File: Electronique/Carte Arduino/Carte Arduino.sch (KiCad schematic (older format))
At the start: 12 parts

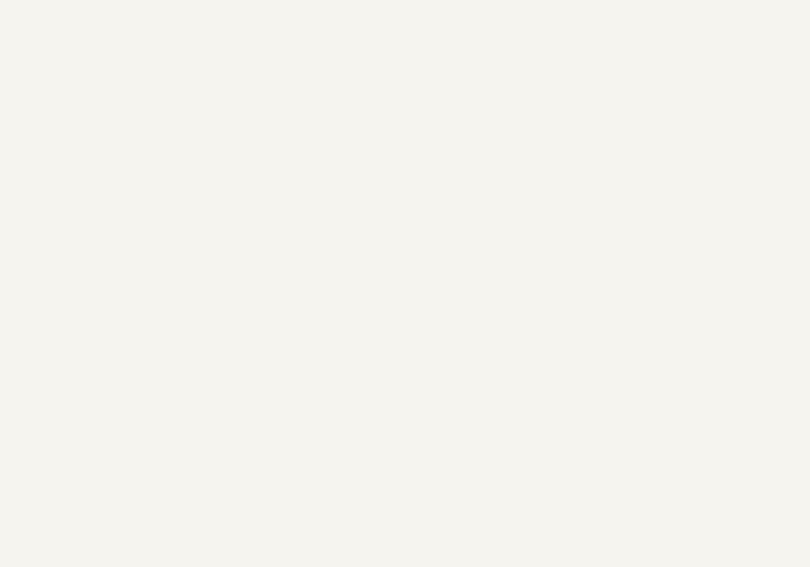
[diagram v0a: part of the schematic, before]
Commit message: Electronique/Carte Arduino/Carte Arduino.sch : - Ajout des connecteurs pour les capteurs de Co2 et de CH4
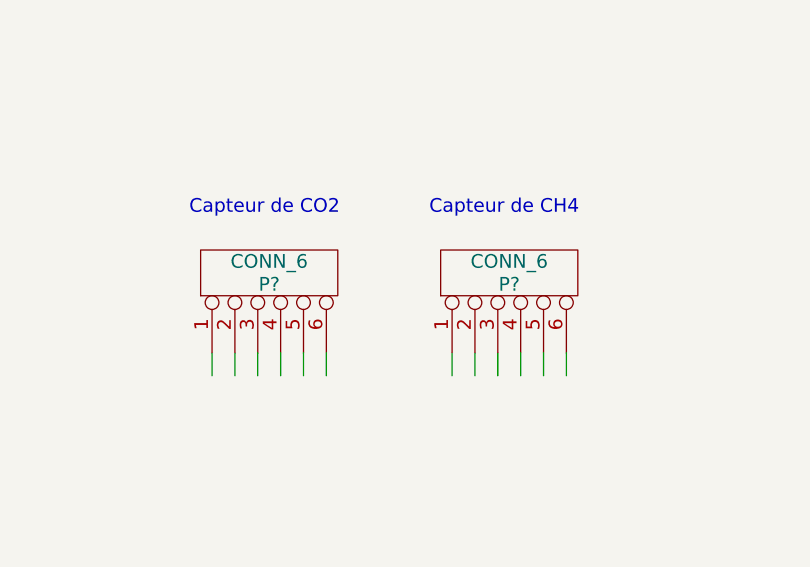
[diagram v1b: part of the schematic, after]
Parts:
- added P? (x2): CONN_6, symbol CONN_6
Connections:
- wire segments 39 -> 51
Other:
- note added: "Capteur de CH4"
- note added: "Capteur de CO2"
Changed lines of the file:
@@
-EESchema Schematic File Version 2  date 12/12/2011 20:48:11
+EESchema Schematic File Version 2  date 12/12/2011 22:18:57
 LIBS:power
 LIBS:device
@@
 Comment4 ""
 $EndDescr
+Wire Wire Line
+	5400 3950 5400 4050
+Wire Wire Line
+	5200 3950 5200 4050
+Wire Wire Line
+	5000 3950 5000 4050
+Wire Wire Line
+	4350 3950 4350 4050
+Wire Wire Line
+	4150 3950 4150 4050
+Wire Wire Line
+	3950 3950 3950 4050
+Wire Wire Line
+	7750 6550 7850 6550
+Wire Wire Line
+	9550 6350 9650 6350
+Wire Wire Line
+	9550 6450 9650 6450
+Wire Wire Line
+	7850 5900 7750 5900
+Wire Wire Line
+	5950 6400 5950 6500
+Wire Wire Line
+	5750 6400 5750 6500
+Wire Wire Line
+	5550 6400 5550 6500
+Wire Wire Line
+	5150 6400 5150 6500
+Wire Wire Line
+	4950 6400 4950 6500
+Wire Wire Line
+	4750 6400 4750 6500
+Wire Wire Line
+	4550 6400 4550 6500
+Wire Wire Line
+	4150 6400 4150 6500
+Wire Wire Line
+	3950 6400 3950 6500
+Wire Wire Line
+	2100 5350 2100 5500
+Wire Wire Line
+	2100 4750 2100 4850
+Wire Wire Line
+	2300 4850 2300 4750
+Wire Wire Line
+	1900 4850 1900 4750
+Wire Wire Line
+	1700 4750 1700 4850
+Wire Wire Line
+	1700 5350 1700 5500
+Wire Wire Line
+	1300 5350 1300 5500
+Wire Wire Line
+	1300 4750 1300 4850
+Wire Wire Line
+	1500 4850 1500 4750
+Wire Wire Line
+	1100 4850 1100 4750
+Wire Wire Line
+	900  4750 900  4850
+Wire Wire Line
+	900  5350 900  5500
+Wire Wire Line
+	3850 6400 3850 6500
+Wire Wire Line
+	4050 6400 4050 6500
+Wire Wire Line
+	4450 6400 4450 6500
+Wire Wire Line
+	4650 6400 4650 6500
+Wire Wire Line
+	4850 6400 4850 6500
+Wire Wire Line
+	5050 6400 5050 6500
+Wire Wire Line
+	5450 6400 5450 6500
+Wire Wire Line
+	5650 6400 5650 6500
+Wire Wire Line
+	5850 6400 5850 6500
+Wire Wire Line
+	6050 6400 6050 6500
+Wire Wire Line
+	6150 6400 6150 6500
+Wire Wire Line
+	9550 6500 9650 6500
+Wire Wire Line
+	9550 6400 9650 6400
+Wire Wire Line
+	7850 6500 7750 6500
+Wire Wire Line
+	3850 3950 3850 4050
+Wire Wire Line
+	4050 3950 4050 4050
+Wire Wire Line
+	4250 3950 4250 4050
+Wire Wire Line
+	4900 3950 4900 4050
+Wire Wire Line
+	5100 3950 5100 4050
+Wire Wire Line
+	5300 3950 5300 4050
+Text Notes 4800 3350 0    60   ~ 0
+Capteur de CH4
+Text Notes 3750 3350 0    60   ~ 0
+Capteur de CO2
+$Comp
+L CONN_6 P?
+U 1 1 4EE66058
+P 5150 3600
+F 0 "P?" V 5100 3600 60  0000 C CNN
+F 1 "CONN_6" V 5200 3600 60  0000 C CNN
+	1    5150 3600
+	0    -1   -1   0
+$EndComp
+$Comp
+L CONN_6 P?
+U 1 1 4EE66049
+P 4100 3600
+F 0 "P?" V 4050 3600 60  0000 C CNN
+F 1 "CONN_6" V 4150 3600 60  0000 C CNN
+	1    4100 3600
+	0    -1   -1   0
+$EndComp
 NoConn ~ 5950 6500
 NoConn ~ 5850 6500
@@
 Text Notes 8550 5750 0    60   ~ 0
 Arduino
-Wire Wire Line
-	7750 6550 7850 6550
-Wire Wire Line
-	9550 6350 9650 6350
-Wire Wire Line
-	9550 6450 9650 6450
-Wire Wire Line
-	7850 5900 7750 5900
-Wire Wire Line
-	5950 6400 5950 6500
-Wire Wire Line
-	5750 6400 5750 6500
-Wire Wire Line
-	5550 6400 5550 6500
-Wire Wire Line
-	5150 6400 5150 6500
-Wire Wire Line
-	4950 6400 4950 6500
-Wire Wire Line
-	4750 6400 4750 6500
-Wire Wire Line
-	4550 6400 4550 6500
-Wire Wire Line
-	4150 6400 4150 6500
-Wire Wire Line
-	3950 6400 3950 6500
-Wire Wire Line
-	2100 5350 2100 5500
-Wire Wire Line
-	2100 4750 2100 4850
-Wire Wire Line
-	2300 4850 2300 4750
-Wire Wire Line
-	1900 4850 1900 4750
-Wire Wire Line
-	1700 4750 1700 4850
-Wire Wire Line
-	1700 5350 1700 5500
-Wire Wire Line
-	1300 5350 1300 5500
-Wire Wire Line
-	1300 4750 1300 4850
-Wire Wire Line
-	1500 4850 1500 4750
-Wire Wire Line
-	1100 4850 1100 4750
-Wire Wire Line
-	900  4750 900  4850
-Wire Wire Line
-	900  5350 900  5500
-Wire Wire Line
-	3850 6400 3850 6500
-Wire Wire Line
-	4050 6400 4050 6500
-Wire Wire Line
-	4450 6400 4450 6500
-Wire Wire Line
-	4650 6400 4650 6500
-Wire Wire Line
-	4850 6400 4850 6500
-Wire Wire Line
-	5050 6400 5050 6500
-Wire Wire Line
-	5450 6400 5450 6500
-Wire Wire Line
-	5650 6400 5650 6500
-Wire Wire Line
-	5850 6400 5850 6500
-Wire Wire Line
-	6050 6400 6050 6500
-Wire Wire Line
-	6150 6400 6150 6500
-Wire Wire Line
-	9550 6500 9650 6500
-Wire Wire Line
-	9550 6400 9650 6400
-Wire Wire Line
-	7850 6500 7750 6500
 Text Label 7750 6550 2    60   ~ 0
 Arduino - SCL

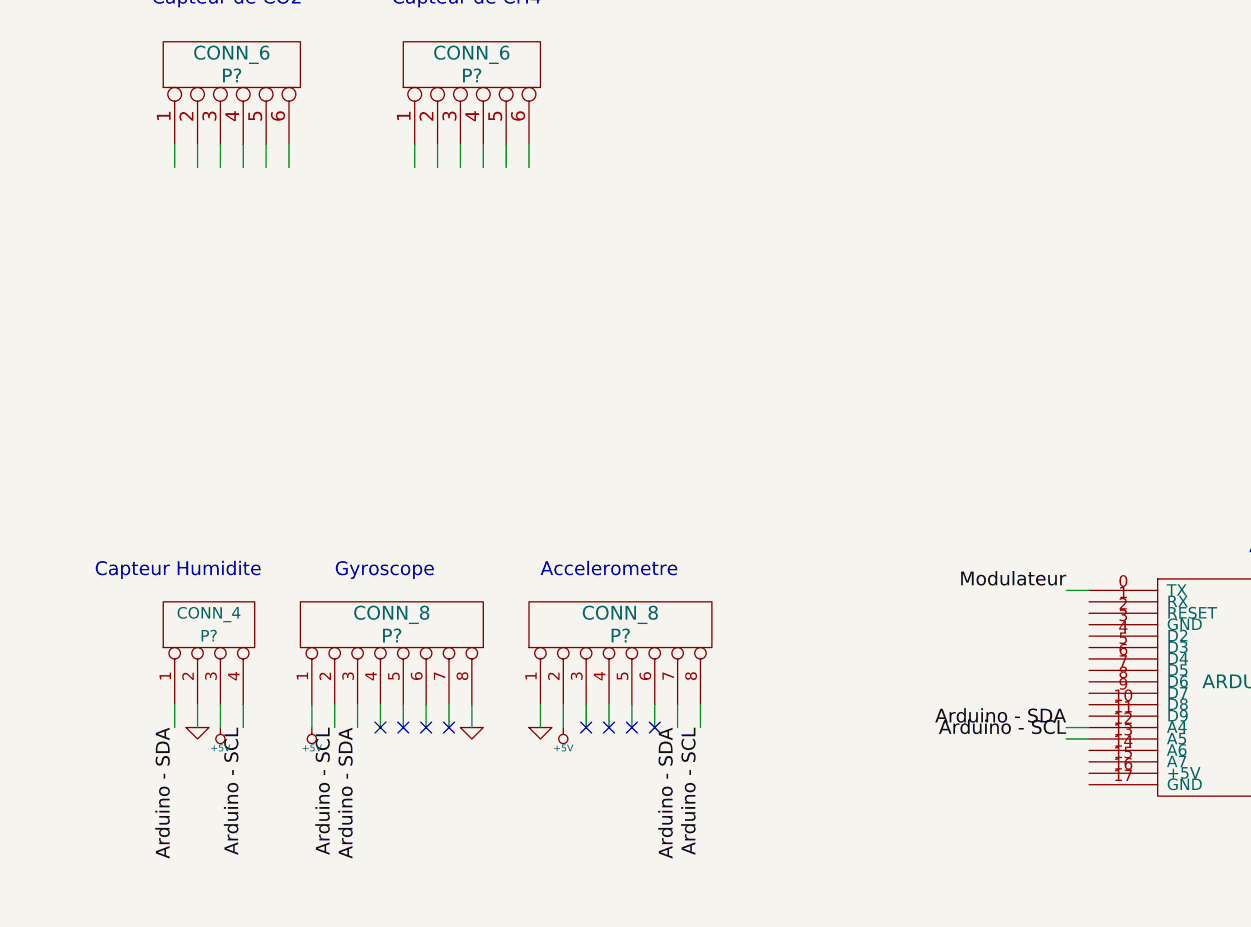
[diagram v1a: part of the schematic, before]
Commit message: Electronique/Carte Arduino/Carte Arduino.sch : - Ajout des connexions des pins des capteurs de CO2 et de CH4
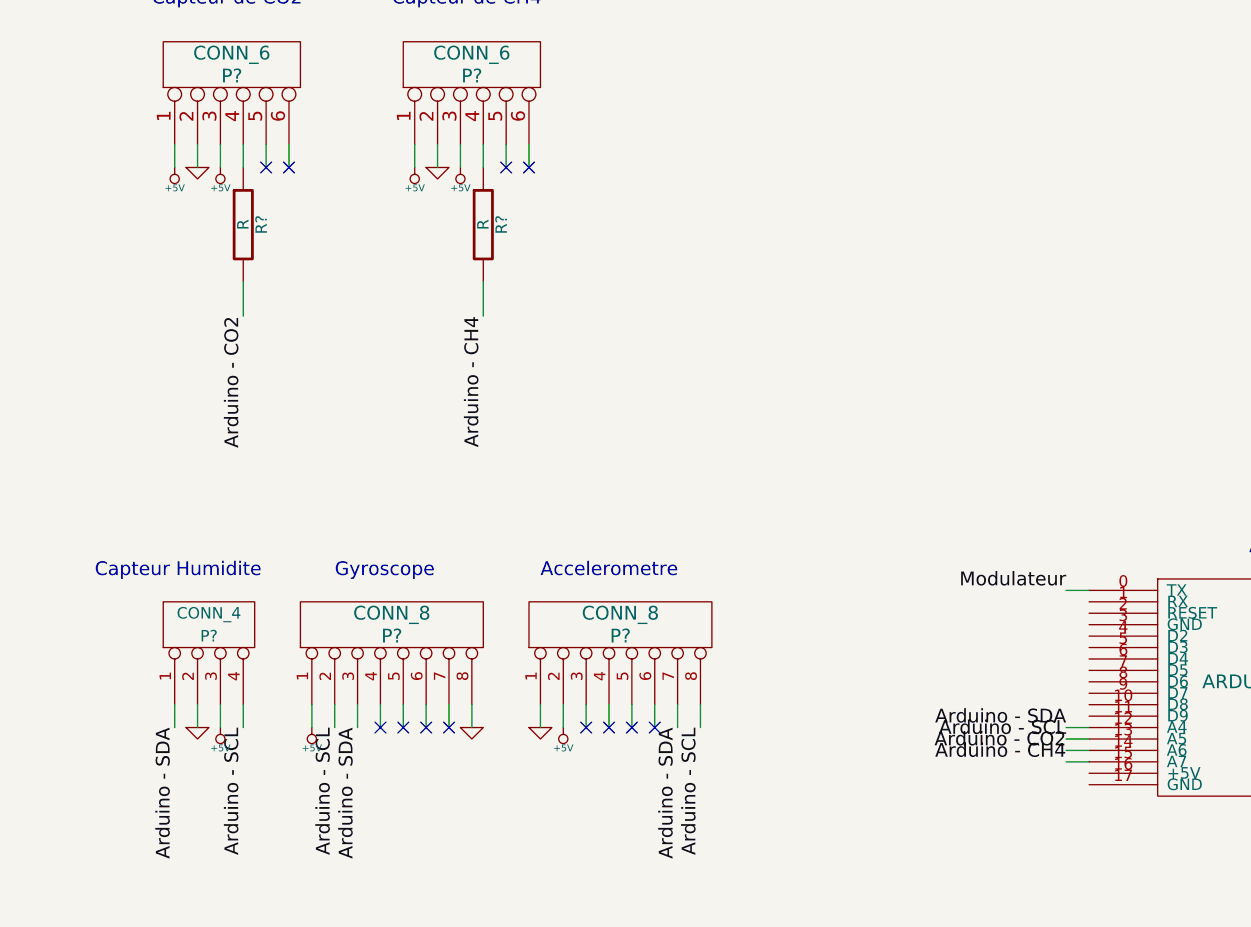
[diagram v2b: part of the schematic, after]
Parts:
- added R? (x2): R, symbol R
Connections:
- net labels added: Arduino - CH4, Arduino - CO2
- wire segments 51 -> 55
- no-connect marks 8 -> 12
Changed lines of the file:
@@
-EESchema Schematic File Version 2  date 12/12/2011 22:18:57
+EESchema Schematic File Version 2  date 13/12/2011 07:36:52
 LIBS:power
 LIBS:device
@@
 Sheet 1 1
 Title ""
-Date "12 dec 2011"
+Date "13 dec 2011"
 Rev ""
 Comp ""
@@
 Comment4 ""
 $EndDescr
+NoConn ~ 5400 4050
+NoConn ~ 5300 4050
+NoConn ~ 4350 4050
+NoConn ~ 4250 4050
+Wire Wire Line
+	7850 6650 7750 6650
+Wire Wire Line
+	5200 4550 5200 4700
+Wire Wire Line
+	4150 4550 4150 4700
 Wire Wire Line
 	5400 3950 5400 4050
@@
 Wire Wire Line
 	5300 3950 5300 4050
+Wire Wire Line
+	7850 6600 7750 6600
+Text Label 7750 6650 2    60   ~ 0
+Arduino - CH4
+Text Label 7750 6600 2    60   ~ 0
+Arduino - CO2
+Text Label 5200 4700 3    60   ~ 0
+Arduino - CH4
+$Comp
+L R R?
+U 1 1 4EE6F1CD
+P 5200 4300
+F 0 "R?" V 5280 4300 50  0000 C CNN
+F 1 "R" V 5200 4300 50  0000 C CNN
+	1    5200 4300
+	1    0    0    -1
+$EndComp
+$Comp
+L R R?
+U 1 1 4EE6F1C1
+P 4150 4300
+F 0 "R?" V 4230 4300 50  0000 C CNN
+F 1 "R" V 4150 4300 50  0000 C CNN
+	1    4150 4300
+	1    0    0    -1
+$EndComp
+Text Label 4150 4700 3    60   ~ 0
+Arduino - CO2
+$Comp
+L +5V #PWR?
+U 1 1 4EE6F1B0
+P 5100 4050
+F 0 "#PWR?" H 5100 4140 20  0001 C CNN
+F 1 "+5V" H 5100 4140 30  0000 C CNN
+	1    5100 4050
+	-1   0    0    1
+$EndComp
+$Comp
+L +5V #PWR?
+U 1 1 4EE6F1A6
+P 4050 4050
+F 0 "#PWR?" H 4050 4140 20  0001 C CNN
+F 1 "+5V" H 4050 4140 30  0000 C CNN
+	1    4050 4050
+	-1   0    0    1
+$EndComp
+$Comp
+L GND #PWR?
+U 1 1 4EE6F197
+P 5000 4050
+F 0 "#PWR?" H 5000 4050 30  0001 C CNN
+F 1 "GND" H 5000 3980 30  0001 C CNN
+	1    5000 4050
+	1    0    0    -1
+$EndComp
+$Comp
+L GND #PWR?
+U 1 1 4EE6F192
+P 3950 4050
+F 0 "#PWR?" H 3950 4050 30  0001 C CNN
+F 1 "GND" H 3950 3980 30  0001 C CNN
+	1    3950 4050
+	1    0    0    -1
+$EndComp
+$Comp
+L +5V #PWR?
+U 1 1 4EE6F18C
+P 4900 4050
+F 0 "#PWR?" H 4900 4140 20  0001 C CNN
+F 1 "+5V" H 4900 4140 30  0000 C CNN
+	1    4900 4050
+	-1   0    0    1
+$EndComp
+$Comp
+L +5V #PWR?
+U 1 1 4EE6F184
+P 3850 4050
+F 0 "#PWR?" H 3850 4140 20  0001 C CNN
+F 1 "+5V" H 3850 4140 30  0000 C CNN
+	1    3850 4050
+	-1   0    0    1
+$EndComp
 Text Notes 4800 3350 0    60   ~ 0
 Capteur de CH4
